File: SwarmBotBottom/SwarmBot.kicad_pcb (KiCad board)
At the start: 2 copper layers, 41 x 50 mm, 43 parts, among them J1 Conn_01x04_Male, J2 Conn_01x04_Male, J6 Conn_01x08_Female, U1 STSPIN220, U2 STSPIN220, U4 MCP73831-2-OT

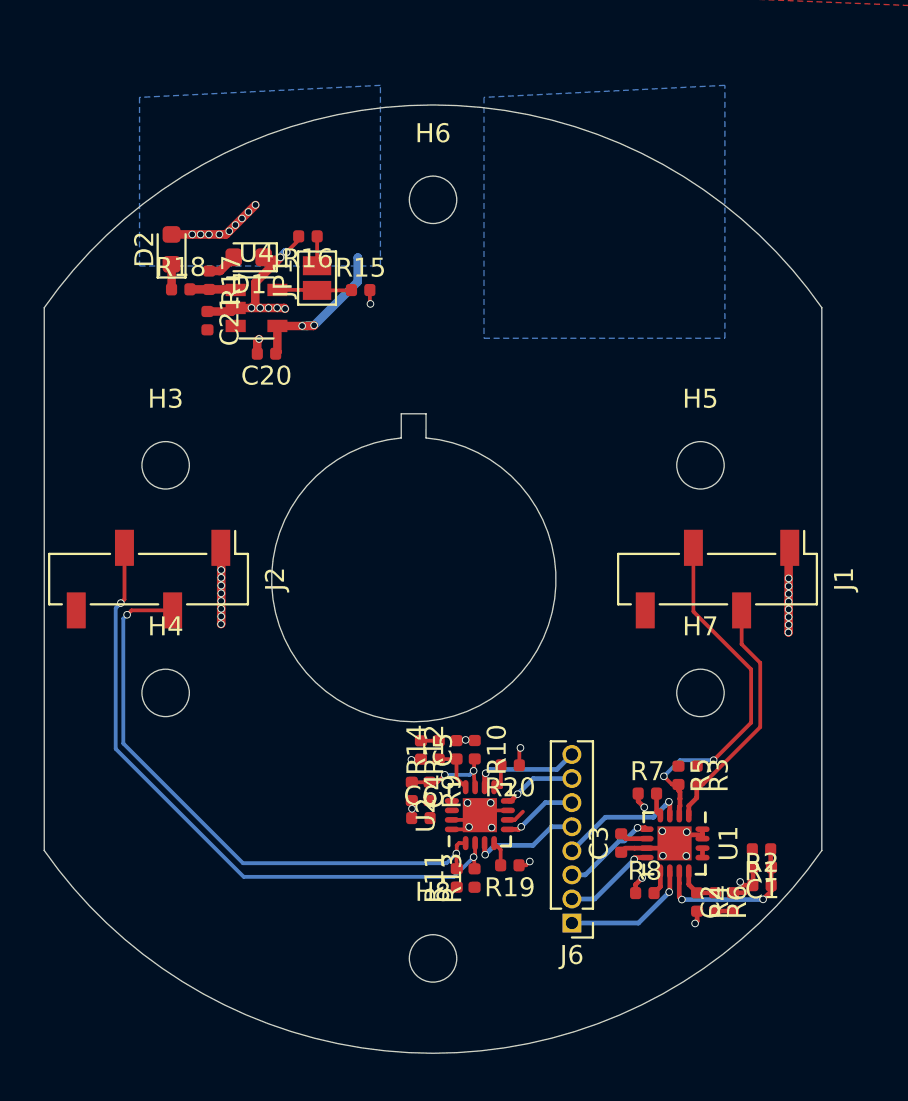
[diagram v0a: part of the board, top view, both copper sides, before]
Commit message: Camera routing with all sensors and motors
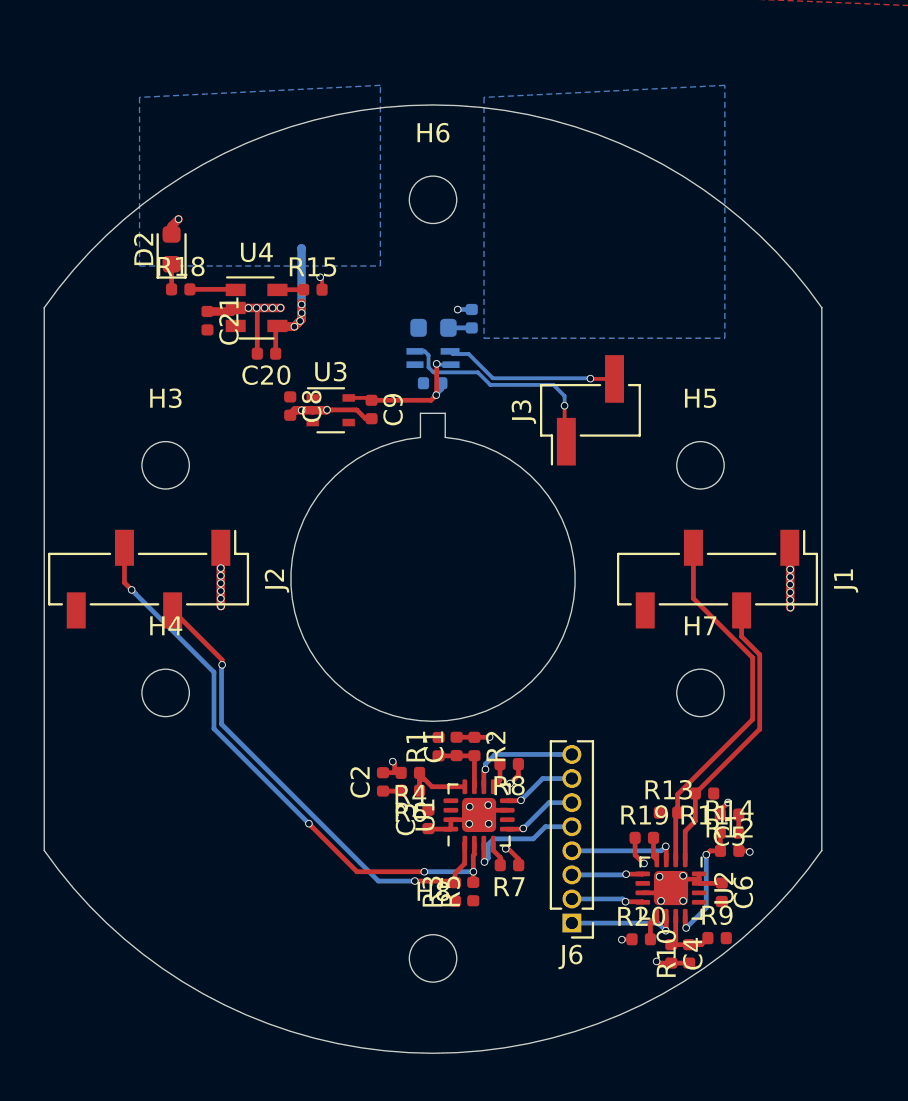
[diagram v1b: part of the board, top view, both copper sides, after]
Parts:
- removed D1: LED, LED_SMD:LED_0603_1608Metric
- removed JP1: Jumper_NO_Small, Jumper:SolderJumper-2_P1.3mm_Open_Pad1.0x1.5mm
- removed R16, R17: R, Resistor_SMD:R_0402_1005Metric
- added C7: C, Capacitor_SMD:C_0402_1005Metric, B.Cu at (-0.02, -10.3)
- added C8: C, Capacitor_SMD:C_0402_1005Metric, F.Cu at (-7.53, -9.12)
- added C9: C, Capacitor_SMD:C_0402_1005Metric, F.Cu at (-3.24, -8.94)
- added D3: LED, LED_SMD:LED_0603_1608Metric, B.Cu at (0.02, -13.2)
- added IC1: VEML6040A3OG, VEML6040A3OG:VEML6040A3OG, B.Cu at (0.00, -11.7)
- added J3: Conn_01x02_Male, Connector_PinHeader_2.54mm:PinHeader_1x02_P2.54mm_Vertical_SMD_Pin1Left, F.Cu at (8.30, -8.90)
- added R21: R, Resistor_SMD:R_0402_1005Metric, B.Cu at (2.04, -13.7)
- added U3: MIC5366-3.3YC5, Package_TO_SOT_SMD:SOT-353_SC-70-5, F.Cu at (-5.39, -8.90)
- C1, C4: value C -> 0.1uF
- C2, C5: value C -> 22nF
- C3, C6: value C -> 1uF
- R11, R13, R3, R5: value R -> 10K
- R12, R4: value R -> 10k
- R14, R6: value R -> 1K
- R19, R20, R7, R8: value R -> 200m
- U1, U2: footprint Package_DFN_QFN:QFN-16-1EP_3x3mm_P0.5mm_EP1.8x1.8mm -> Package_DFN_QFN:VQFN-16-1EP_3x3mm_P0.5mm_EP1.8x1.8mm
- moved C2 19.5 mm to (-2.64, 10.7)
- moved R1 17.9 mm to (0.29, 8.83), turned to 90 degrees
- moved C1 17.3 mm to (1.24, 8.82), turned to 90 degrees
- moved R6 17.1 mm to (-1.19, 11.2), turned to 180 degrees
- moved R9 17.0 mm to (15.0, 18.9), turned to 0 degrees
- moved R2 16.8 mm to (2.18, 8.83), turned to 270 degrees
- moved C5 16.6 mm to (15.6, 12.4), turned to 180 degrees
- moved R4 16.6 mm to (-1.20, 10.2), turned to 180 degrees
- moved C6 16.3 mm to (15.2, 16.5), turned to 270 degrees
- moved C4 16.1 mm to (12.6, 19.8)
- moved R14 15.9 mm to (15.6, 13.4), turned to 0 degrees
- moved R10 15.6 mm to (13.5, 19.8), turned to 90 degrees
- moved R12 15.4 mm to (15.6, 14.3), turned to 0 degrees
- moved R3 14.1 mm to (1.16, 16.5), turned to 90 degrees
- moved R11 13.8 mm to (14.3, 11.3), turned to 180 degrees
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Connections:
- R11 pad 2: /Sheet5DAF9EF1/M2DIR -> /Sheet5DAF9EF1/M1DIR
- R13 pad 2: /Sheet5DAF9EF1/M2STEP -> /Sheet5DAF9EF1/M1STEP
- R3 pad 2: /Sheet5DAF9EF1/M1DIR -> /Sheet5DAF9EF1/M2DIR
- R5 pad 2: /Sheet5DAF9EF1/M1STEP -> /Sheet5DAF9EF1/M2STEP
- U1 pad 1: /Sheet5DAF9EF1/M1DIR -> /Sheet5DAF9EF1/M2DIR
- U1 pad 10: /Sheet5DAF9EF1/B1 -> /Sheet5DAF9EF1/B1_2
- U1 pad 2: /Sheet5DAF9EF1/M1STEP -> /Sheet5DAF9EF1/M2STEP
- U1 pad 3: /Sheet5DAF9EF1/A1 -> /Sheet5DAF9EF1/A1_2
- U1 pad 5: /Sheet5DAF9EF1/A2 -> /Sheet5DAF9EF1/A2_2
- U1 pad 8: /Sheet5DAF9EF1/B2 -> /Sheet5DAF9EF1/B2_2
- U2 pad 1: /Sheet5DAF9EF1/M2DIR -> /Sheet5DAF9EF1/M1DIR
- U2 pad 10: /Sheet5DAF9EF1/B1_2 -> /Sheet5DAF9EF1/B1
- U2 pad 2: /Sheet5DAF9EF1/M2STEP -> /Sheet5DAF9EF1/M1STEP
- U2 pad 3: /Sheet5DAF9EF1/A1_2 -> /Sheet5DAF9EF1/A1
- U2 pad 5: /Sheet5DAF9EF1/A2_2 -> /Sheet5DAF9EF1/A2
- U2 pad 8: /Sheet5DAF9EF1/B2_2 -> /Sheet5DAF9EF1/B2
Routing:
- net /Sheet5DAF9EF1/SDA: track 0.00 -> 11.7 mm, vias 0 -> 1
- net /Sheet5DAF9EF1/SCL: track 0.00 -> 9.27 mm, vias 0 -> 1
- net +3V3: track 0.00 -> 7.96 mm, vias 0 -> 2
- net /Sheet5DAF9EF1/M2DIR: track 31.5 -> 25.1 mm
- net Net-(C1-Pad1): track 8.66 -> 3.53 mm, vias 2 -> 0
- net +5V: track 13.7 -> 9.09 mm, vias 11 -> 5
- net Net-(R12-Pad1): track 2.63 -> 6.74 mm, vias 0 -> 2
- net /Sheet5DAF9EF1/M2STEP: track 34.3 -> 30.4 mm, vias 2 -> 4
- net Net-(R15-Pad1): track 3.92 -> 1.40 mm
- net /Sheet5DAF9EF1/M1DIR: track 13.0 -> 15.2 mm
- net +BATT: track 2.92 -> 0.74 mm, vias 0 -> 1
- net Net-(D1-Pad2): track 1.60 -> 0.00 mm
- net Net-(JP1-Pad2): track 1.55 -> 0.00 mm
- net Net-(C4-Pad1): track 5.01 -> 3.66 mm, vias 2 -> 0
- net /Sheet5DAF9EF1/A2: track 5.00 -> 3.76 mm
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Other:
- outline, holes or cut-outs redrawn
- net class Default: clearance 0.2 -> 0.127
- rule trace_clearance: 0.2 -> 0.127

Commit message: V1 ready to order
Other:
- board text added: "Keion Bisland 2019"
- board text added: "SwarmBot V1 Bottom Board"

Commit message: things
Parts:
- added C10: C, Capacitor_SMD:C_0402_1005Metric, F.Cu at (8.74, -13.4)
- added D1: LED, LED_SMD:LED_0603_1608Metric, B.Cu at (0.00, 13.0)
- added D4: LED, LED_SMD:LED_0603_1608Metric, F.Cu at (6.72, -18.4)
- added D5: LED, LED_SMD:LED_0603_1608Metric, B.Cu at (0.00, 11.0)
- added IC2: PCA9570GMH, PCA9570GMH:PCA9570GMH, F.Cu at (6.96, -13.9)
- added R16: R, Resistor_SMD:R_0402_1005Metric, B.Cu at (0.32, 14.3)
- added R17: R, Resistor_SMD:R_0402_1005Metric, F.Cu at (6.50, -17.1)
- added R22: R, Resistor_SMD:R_0402_1005Metric, B.Cu at (0.23, 9.80)
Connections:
- R21 pad 2: +BATT -> /Sheet5DAF9EF1/WHITELED
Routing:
- net /Sheet5DAF9EF1/UVLED: track 0.00 -> 34.7 mm, vias 0 -> 1
- net /Sheet5DAF9EF1/IRLED: track 0.00 -> 34.2 mm, vias 0 -> 1
- net +3V3: track 7.96 -> 18.3 mm, vias 2 -> 4
- net /Sheet5DAF9EF1/WHITELED: track 0.00 -> 6.36 mm, vias 0 -> 1
- net /Sheet5DAF9EF1/SDA: track 11.7 -> 16.0 mm, vias 1 -> 2
- net /Sheet5DAF9EF1/SCL: track 9.27 -> 12.5 mm, vias 1 -> 2
- net GND: track 38.8 -> 41.6 mm, vias 37 -> 40
- net /Sheet5DAF9EF1/POWERLED: track 0.00 -> 2.62 mm
- net Net-(D4-Pad2): track 0.00 -> 1.34 mm
- net Net-(D1-Pad2): track 0.00 -> 1.31 mm
- net Net-(D5-Pad2): track 0.00 -> 1.23 mm
- net +BATT: track 0.74 -> 0.00 mm, vias 1 -> 0

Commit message: Final Design
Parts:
- removed D3: LED, LED_SMD:LED_0603_1608Metric
- removed R10, R2, R21: R, Resistor_SMD:R_0402_1005Metric
- added C11: 10uF, Capacitor_SMD:C_0402_1005Metric, F.Cu at (-2.20, -16.3)
- added C12: 0.1uF, Capacitor_SMD:C_0402_1005Metric, B.Cu at (7.36, -7.29)
- added IC3: VEML6040A3OG, VEML6040A3OG:VEML6040A3OG, B.Cu at (-7.00, -9.00)
- added U5: TCA9548AMRGER, Package_DFN_QFN:Texas_RGE0024C_EP2.1x2.1mm, F.Cu at (-0.10, -13.0)
- C10, C7: value C -> 0.1uF
- C20, C21, C8, C9: value C -> 1uF
- D1, D2, D4: value LED -> WHITE
- D5: value LED -> UV
- IC2: value PCA9570GMH -> PCA9532BS,118; footprint PCA9570GMH:PCA9570GMH -> Package_DFN_QFN:VQFN-24-1EP_4x4mm_P0.5mm_EP2.45x2.45mm
- J1, J2: footprint Connector_PinSocket_2.54mm:PinSocket_1x04_P2.54mm_Vertical_SMD_Pin1Left -> Connector_PinSocket_2.54mm:PinSocket_1x04_P2.54mm_Vertical_SMD_Pin1Right
- J3: footprint Connector_PinHeader_2.54mm:PinHeader_1x02_P2.54mm_Vertical_SMD_Pin1Left -> Connector_PinHeader_2.54mm:PinHeader_1x02_P2.54mm_Vertical_SMD_Pin1Right
- R1, R9: value R -> 1K
- R15, R18: value R -> 470R
- R16, R17, R22: value R -> 330R
- moved IC1 7.49 mm to (7.00, -9.00)
- moved D4 7.43 mm to (13.4, -15.1), turned to 90 degrees
- moved C7 7.22 mm to (-6.59, -7.34)
- moved R17 6.32 mm to (12.8, -17.2), turned to 180 degrees
- moved IC2 3.31 mm to (8.29, -16.9), turned to 180 degrees
- moved R9 1.02 mm to (14.0, 19.0)
- moved C1 0.84 mm to (1.98, 9.24)
- moved R1 0.81 mm to (1.00, 9.24)
- moved R20 0.71 mm to (10.7, 19.6), turned to 90 degrees
- moved R19 0.65 mm to (10.6, 13.3)
- moved C3 0.54 mm to (-0.74, 12.9)
- moved R7 0.46 mm to (3.98, 15.5)
- moved D1 0.42 mm to (-0.01, 12.6)
- moved C10 0.12 mm to (8.73, -13.5), turned to 180 degrees
- moved U3 0.10 mm to (-5.40, -9.00)
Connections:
- C10 pad 1: +3V3 -> GND
- C10 pad 2: GND -> +3V3
- IC1 pad 2: /Sheet5DAF9EF1/SDA -> /Sheet5DAF9EF1/SDA1
- IC1 pad 3: /Sheet5DAF9EF1/SCL -> /Sheet5DAF9EF1/SCL1
- IC2 pad 1: /Sheet5DAF9EF1/WHITELED -> /Sheet5DAF9EF1/IRLED
- IC2 pad 2: /Sheet5DAF9EF1/POWERLED -> /Sheet5DAF9EF1/UVLED
- IC2 pad 3: /Sheet5DAF9EF1/UVLED -> /Sheet5DAF9EF1/POWERLED
- IC2 pad 4: GND -> (no net)
- IC2 pad 5: /Sheet5DAF9EF1/IRLED -> /Sheet5DAF9EF1/STEPPERENL
- IC2 pad 6: /Sheet5DAF9EF1/SCL -> /Sheet5DAF9EF1/CURRSETL
- IC2 pad 7: /Sheet5DAF9EF1/SDA -> (no net)
- IC2 pad 8: +3V3 -> (no net)
- R1 pad 2: +BATT -> /Sheet5DAF9EF1/CURRSETR
- R9 pad 2: +BATT -> /Sheet5DAF9EF1/CURRSETL
- U1 pad 13: +BATT -> /Sheet5DAF9EF1/STEPPERENR
- U2 pad 13: +BATT -> /Sheet5DAF9EF1/STEPPERENL
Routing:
- net /Sheet5DAF9EF1/CURRSETL: track 0.00 -> 46.6 mm, vias 0 -> 2
- net /Sheet5DAF9EF1/STEPPERENL: track 0.00 -> 46.1 mm, vias 0 -> 2
- net /Sheet5DAF9EF1/STEPPERENR: track 0.00 -> 40.9 mm, vias 0 -> 2
- net /Sheet5DAF9EF1/CURRSETR: track 0.00 -> 34.7 mm, vias 0 -> 2
- net +BATT: track 0.00 -> 18.2 mm, vias 0 -> 20
- net +3V3: track 18.3 -> 3.42 mm, vias 4 -> 2
- net /Sheet5DAF9EF1/M2DIR: track 25.1 -> 35.6 mm, vias 2 -> 0
- net /Sheet5DAF9EF1/SCL1: track 0.00 -> 9.18 mm, vias 0 -> 3
- net /Sheet5DAF9EF1/SDA2: track 0.00 -> 7.14 mm, vias 0 -> 1
- net /Sheet5DAF9EF1/WHITELED: track 6.36 -> 0.00 mm, vias 1 -> 0
- net /Sheet5DAF9EF1/SDA1: track 0.00 -> 5.43 mm, vias 0 -> 1
- net /Sheet5DAF9EF1/SCL2: track 0.00 -> 5.32 mm, vias 0 -> 1
- net /Sheet5DAF9EF1/IRLED: track 34.2 -> 39.4 mm, vias 1 -> 3
- net /Sheet5DAF9EF1/M1DIR: track 15.2 -> 19.2 mm
- net /Sheet5DAF9EF1/M2STEP: track 30.4 -> 34.1 mm, vias 4 -> 2
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- added copper zone on F.Cu, net +3V3
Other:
- outline, holes or cut-outs redrawn
- board text added: "Keion Bisland 2020"
- board text added: "SwarmBot V1.1 Bottom Board"
- board text removed: "Keion Bisland 2019"
- board text removed: "SwarmBot V1 Bottom Board"

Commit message: Updated LED drivers
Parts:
- IC2: value PCA9532BS,118 -> MAX7313ATG+; footprint Package_DFN_QFN:VQFN-24-1EP_4x4mm_P0.5mm_EP2.45x2.45mm -> MAX7313ATG+:QFN50P400X400X80-25N
- moved IC2 0.08 mm to (8.33, -17.0)
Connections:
- IC2 pad 18: (no net) -> +3V3
- IC2 pad 22: +3V3 -> (no net)
- IC2 pad 23: +3V3 -> GND
- IC2 pad 9: (no net) -> GND
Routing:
- net GND: track 42.8 -> 44.9 mm
